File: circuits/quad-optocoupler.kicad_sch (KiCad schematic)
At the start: 6 parts, among them U3 TLP291-4

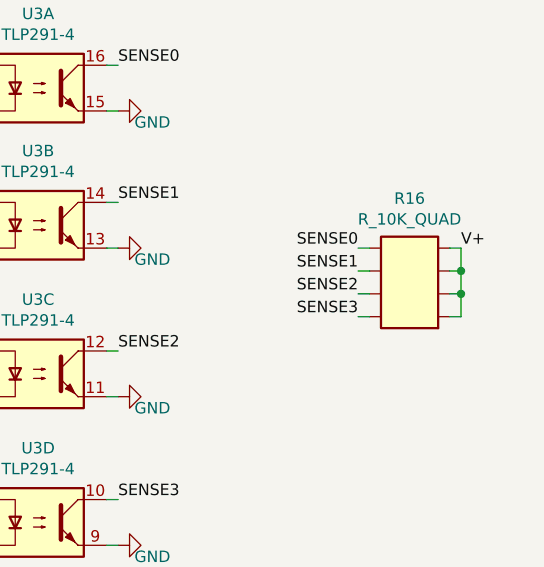
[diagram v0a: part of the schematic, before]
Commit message: corrected footprints for manufacturer
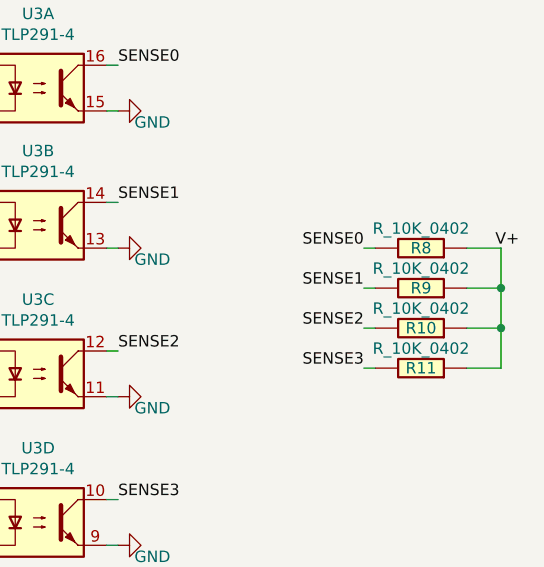
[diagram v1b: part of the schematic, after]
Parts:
- removed R16: R_10K_QUAD, Resistor_SMD:R_Array_Concave_4x0402, symbol Open_Automation:R_10K_QUAD
- added R10, R11, R8, R9: R_10K_0402, Resistor_SMD:R_0402_1005Metric_Pad0.72x0.64mm_HandSolder, symbol Open Automation:R_10K_0402
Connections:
- net SENSE0: now also R8.2
- net SENSE1: now also R9.2
- net SENSE2: now also R10.2
- net SENSE3: now also R11.2
- net V+: now also R10.1, R11.1, R8.1, R9.1
